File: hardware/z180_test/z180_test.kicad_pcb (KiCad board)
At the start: 2 copper layers, 48 parts, among them J1 Conn_01x04, J2 DIN41612_02x32_AB, J3 Conn_01x04, J4 Conn_01x06, J5 Conn_01x06, J6 Conn_02x17_Counter_Clockwise, SW1 SW_Push, U1 74AHC32, U10 8255A, U11 28C256, U12 AS6C4008-55PCN, U2 74LS244, U3 74LS244, U4 74LS244, U5 74LS245, U6 Z180, U7 74HC04, U8 74LS139, U9 74HC14, X1 OSC 12.288MHz 5V

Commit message: tentative placement
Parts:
- added C12: .01uF, Capacitor_THT:C_Disc_D5.0mm_W2.5mm_P2.50mm, F.Cu at (144.8, 45.7)
- added C13: .01uF, Capacitor_THT:C_Disc_D5.0mm_W2.5mm_P2.50mm, F.Cu at (132.0, 43.2)
- added C14: .01uF, Capacitor_THT:C_Disc_D5.0mm_W2.5mm_P2.50mm, F.Cu at (119.4, 45.7)
- X1: value OSC 12.288MHz 5V -> ACO-xxxMHz-A; footprint Oscillator:Oscillator_SeikoEpson_SG-8002DC -> Oscillator:Oscillator_DIP-14
- moved SW1 129.8 mm to (181.6, 38.1)
- moved J1 115.2 mm to (59.7, 36.8), turned to 90 degrees
- moved C11 108.9 mm to (177.8, 58.4), turned to 180 degrees
- moved C5 107.0 mm to (157.5, 45.7), turned to 180 degrees
- moved D3 101.3 mm to (129.5, 33.0)
- moved J4 100.0 mm to (88.9, 137.2), turned to 90 degrees
- moved R10 92.7 mm to (146.1, 38.1), turned to 180 degrees
- moved J5 89.8 mm to (114.3, 137.2), turned to 90 degrees
- moved U5 87.8 mm to (63.5, 106.7), turned to 180 degrees
- moved U10 86.0 mm to (168.9, 63.5)
- moved C8 82.9 mm to (129.5, 38.1)
- moved C10 80.1 mm to (156.2, 73.7), turned to 180 degrees
- moved U8 79.8 mm to (127.0, 48.3)
- moved R12 79.4 mm to (146.1, 121.9), turned to 180 degrees
- moved R1 69.9 mm to (55.9, 123.2)
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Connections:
- X1 pad 8: VCC -> Net-(U6-EXTAL)
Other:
- board outline added: 177.8 x 114.3 mm

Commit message: placement
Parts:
- added H1: MountingHole, MountingHolesInch:Mtg4-40, F.Cu at (27.9, 31.8)
- added H2: MountingHole, MountingHolesInch:Mtg4-40, F.Cu at (27.9, 138.4)
- added H3: MountingHole, MountingHolesInch:Mtg4-40, F.Cu at (240.0, 31.8)
- added H4: MountingHole, MountingHolesInch:Mtg4-40, F.Cu at (240.0, 138.4)
- added H5: MountingHole, MountingHolesInch:Mtg4-40, F.Cu at (86.4, 138.4)
- added H6: MountingHole, MountingHolesInch:Mtg4-40, F.Cu at (86.4, 31.8)
- added H7: MountingHole, MountingHolesInch:Mtg4-40, F.Cu at (153.7, 31.8)
- added H8: MountingHole, MountingHolesInch:Mtg4-40, F.Cu at (195.6, 138.4)
- added J7: DIN41612_02x32_AB, Connector_DIN:DIN41612_B_2x32_Female_Vertical_THT, F.Cu at (35.6, 47.0)
- added J8: DIN41612_02x32_AB, Connector_DIN:DIN41612_B_2x32_Female_Vertical_THT, F.Cu at (54.6, 47.0)
- J1: footprint Connector_PinHeader_2.54mm:PinHeader_1x04_P2.54mm_Vertical -> Connector_Molex:Molex_KK-396_A-41791-0004_1x04_P3.96mm_Vertical
- moved SW1 93.2 mm to (219.7, 123.2)
- moved J1 57.3 mm to (117.0, 34.3), turned to 180 degrees
- moved C5 38.1 mm to (195.6, 45.7)
- moved C7 38.1 mm to (174.0, 69.8)
- moved U9 38.1 mm to (177.8, 50.8)
- moved C9 38.1 mm to (109.3, 78.7)
- moved J5 38.1 mm to (152.4, 137.2)
- moved R11 38.1 mm to (146.1, 121.9)
- moved R3 38.1 mm to (132.1, 71.1)
- moved R4 38.1 mm to (121.9, 118.1)
- moved R5 38.1 mm to (121.9, 121.9)
- moved R6 38.1 mm to (132.1, 125.7)
- moved U6 38.1 mm to (156.2, 92.7)
- moved X1 38.1 mm to (132.1, 49.5)
- moved D1 38.1 mm to (99.1, 134.6)
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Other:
- board size 177.8 x 114.3 mm -> 219.7 x 114.3 mm
- copper layers 2 -> 4

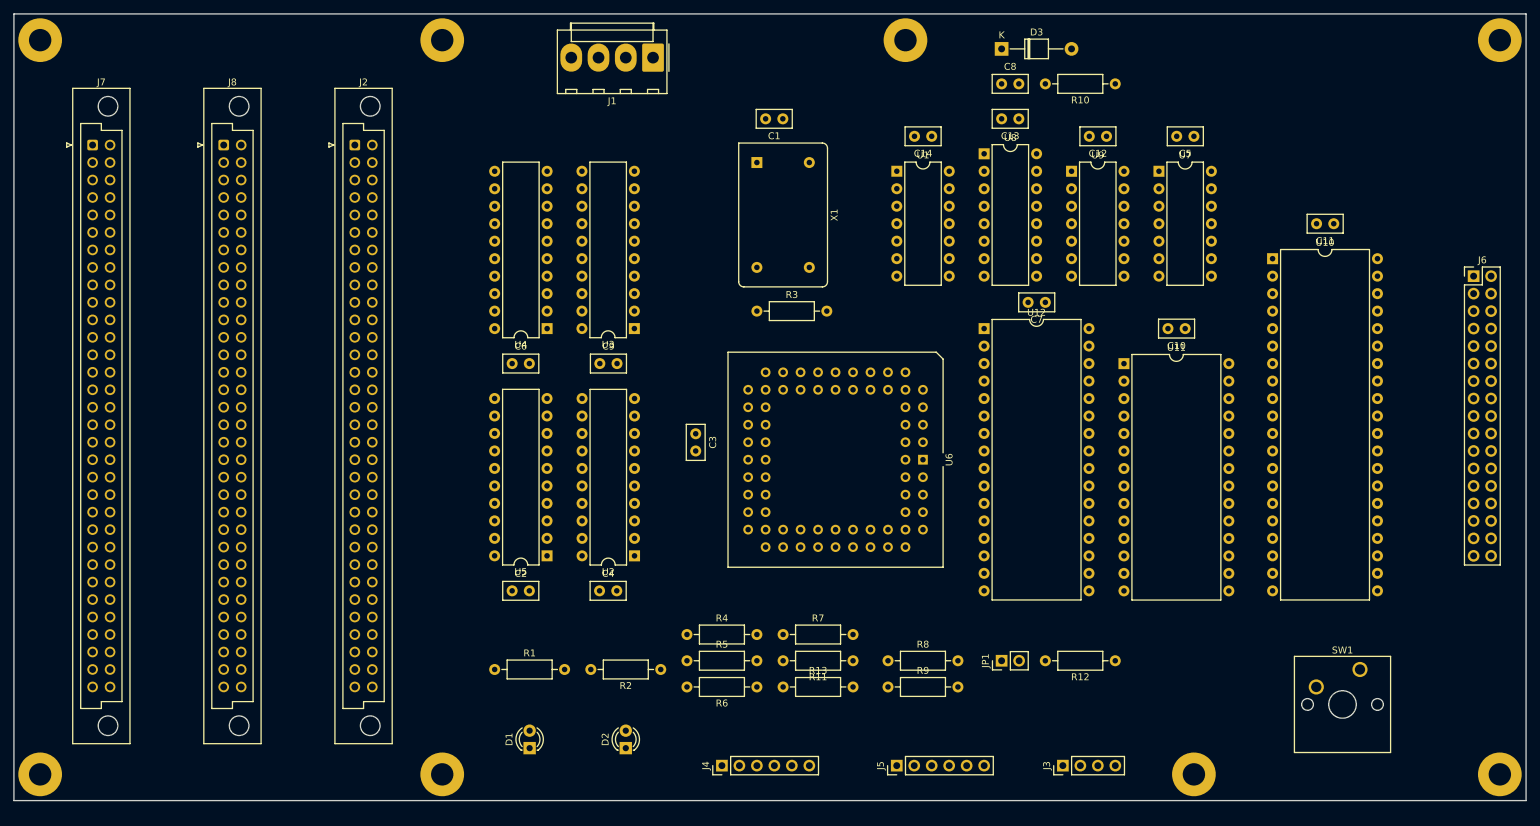
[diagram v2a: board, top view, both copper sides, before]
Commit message: add VR
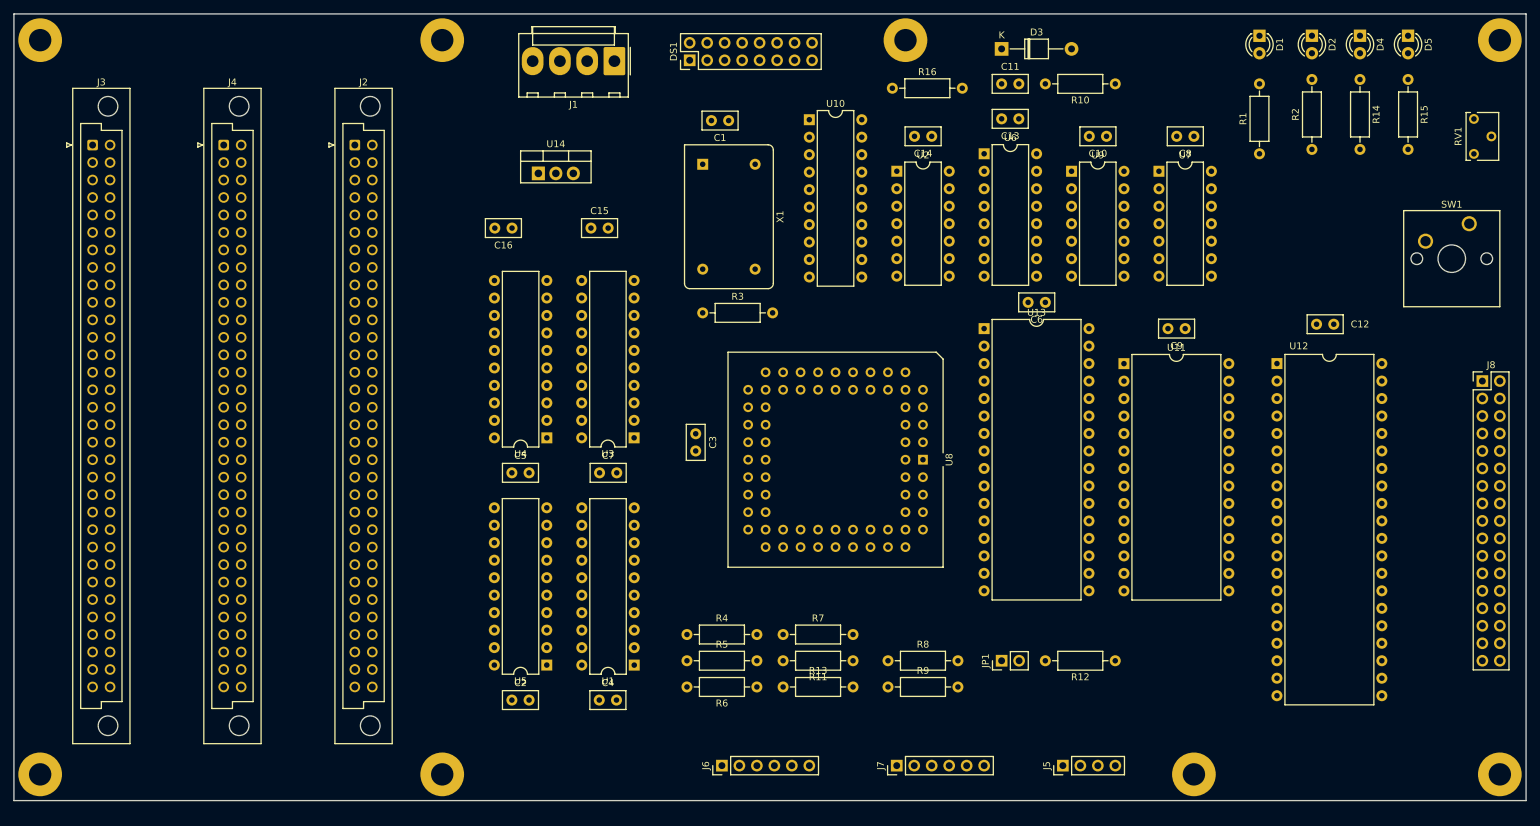
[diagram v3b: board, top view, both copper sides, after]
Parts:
- added C15: .01uF, Capacitor_THT:C_Disc_D5.0mm_W2.5mm_P2.50mm, F.Cu at (108.0, 59.1)
- added C16: .01uF, Capacitor_THT:C_Disc_D5.0mm_W2.5mm_P2.50mm, F.Cu at (96.5, 59.1)
- added D4: LED, LED_THT:LED_D3.0mm, F.Cu at (219.7, 31.1)
- added D5: LED, LED_THT:LED_D3.0mm, F.Cu at (226.7, 31.1)
- added DS1: RC1602A, Connector_PinHeader_2.54mm:PinHeader_2x08_P2.54mm_Vertical, F.Cu at (122.3, 34.7)
- added R14: 1k, Resistor_THT:R_Axial_DIN0207_L6.3mm_D2.5mm_P10.16mm_Horizontal, F.Cu at (219.7, 37.5)
- added R15: 1k, Resistor_THT:R_Axial_DIN0207_L6.3mm_D2.5mm_P10.16mm_Horizontal, F.Cu at (226.7, 37.5)
- added R16: 470, Resistor_THT:R_Axial_DIN0207_L6.3mm_D2.5mm_P10.16mm_Horizontal, F.Cu at (151.8, 38.7)
- added RV1: 10k, Potentiometer_THT:Potentiometer_Bourns_3266W_Vertical, F.Cu at (236.3, 43.2)
- added U10: 74LS374, Package_DIP:DIP-20_W7.62mm, F.Cu at (139.7, 43.3)
- added U14: LM7805_TO220, Package_TO_SOT_THT:TO-220-3_Vertical, F.Cu at (100.3, 51.1)
- moved D1 148.2 mm to (205.1, 31.1), turned to -90 degrees
- moved D2 143.7 mm to (212.7, 31.1), turned to -90 degrees
- moved R1 134.0 mm to (205.1, 48.3), turned to 90 degrees
- moved R2 121.1 mm to (212.7, 47.6), turned to 90 degrees
- moved SW1 66.7 mm to (235.6, 58.4)
- moved C2 15.9 mm to (96.5, 127.6)
- moved C4 15.9 mm to (109.2, 127.6)
- moved C5 15.9 mm to (96.5, 94.6)
- moved C7 15.9 mm to (109.2, 94.6)
- moved U1 15.9 mm to (114.3, 122.6)
- moved U3 15.9 mm to (114.2, 89.5)
- moved U4 15.9 mm to (101.6, 89.5)
- moved U5 15.9 mm to (101.5, 122.5)
- moved J8 15.3 mm to (237.5, 81.3)
- moved U12 15.3 mm to (207.6, 78.7)
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- renumbered C12 to C10, C8 to C11, C11 to C12, C6 to C5, C7 to C6, C9 to C7, C5 to C8, C10 to C9, J7 to J3, J8 to J4, J3 to J5, J4 to J6, J5 to J7, J6 to J8, U2 to U1, U10 to U12, U12 to U13, U1 to U2, U8 to U6, U6 to U8
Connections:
- J1 pad 1: VCC -> Net-(J1-Pin_1)
- J1 pad 2: VCC -> Net-(J1-Pin_1)
- U6 pad 9: unconnected-(U8B-O3-Pad9) -> /nLCD

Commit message: tweaking placement
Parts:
- moved D5 3.70 mm to (228.6, 34.3)
- moved R15 3.70 mm to (228.6, 40.6)
- moved D4 3.42 mm to (221.0, 34.3)
- moved R14 3.42 mm to (221.0, 40.6)
- moved R1 3.24 mm to (204.5, 51.4)
- moved D1 3.24 mm to (204.5, 34.3)
- moved D2 3.17 mm to (212.7, 34.3)
- moved R2 3.17 mm to (212.7, 50.8)
- moved RV1 2.54 mm to (238.8, 43.2)
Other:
- board text added: "HALT"
- board text added: "LED1"
- board text added: "LED2"
- board text added: "LED3"
- board text added: "Port A"
- board text added: "Port B"
- board text added: "RESET"
- board text added: "Sync"
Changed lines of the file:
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@@
 	(footprint "LED_THT:LED_D3.0mm"
 		(layer "F.Cu")
-		(at 226.695 31.11 -90)
+		(at 228.6 34.285 -90)
 		(descr "LED, diameter 3.0mm, 2 pins")
 		(tags "LED diameter 3.0mm 2 pins")
@@
 		(tags "C Disc series Radial pin pitch 2.50mm  diameter 5mm width 2.5mm Capacitor")
 		(property "Reference" "C15"
-			(at 1.25 -2.5 360)
+			(at 1.25 -2.5 0)
 			(layer "F.SilkS")
 			(effects
@@
 		)
 		(property "Value" ".01uF"
-			(at 1.25 2.5 360)
+			(at 1.25 2.5 0)
 			(layer "F.Fab")
 			(effects
@@
 		)
 		(fp_text user "${REFERENCE}"
-			(at 1.25 0 360)
+			(at 1.25 0 0)
 			(layer "F.Fab")
 			(effects
@@
 	(footprint "LED_THT:LED_D3.0mm"
 		(layer "F.Cu")
-		(at 205.105 31.115 -90)
+		(at 204.47 34.29 -90)
 		(descr "LED, diameter 3.0mm, 2 pins")
 		(tags "LED diameter 3.0mm 2 pins")
@@
 	(footprint "LED_THT:LED_D3.0mm"
 		(layer "F.Cu")
-		(at 212.725 31.11 -90)
+		(at 212.725 34.285 -90)
 		(descr "LED, diameter 3.0mm, 2 pins")
 		(tags "LED diameter 3.0mm 2 pins")
@@
 	(footprint "Resistor_THT:R_Axial_DIN0207_L6.3mm_D2.5mm_P10.16mm_Horizontal"
 		(layer "F.Cu")
-		(at 205.105 48.26 90)
+		(at 204.47 51.435 90)
 		(descr "Resistor, Axial_DIN0207 series, Axial, Horizontal, pin pitch=10.16mm, 0.25W = 1/4W, length*diameter=6.3*2.5mm^2, http://cdn-reichelt.de/documents/datenblatt/B400/1_4W%23YAG.pdf")
 		(tags "Resistor Axial_DIN0207 series Axial Horizontal pin pitch 10.16mm 0.25W = 1/4W length 6.3mm diameter 2.5mm")
@@
 	(footprint "Resistor_THT:R_Axial_DIN0207_L6.3mm_D2.5mm_P10.16mm_Horizontal"
 		(layer "F.Cu")
-		(at 212.725 47.625 90)
+		(at 212.725 50.8 90)
 		(descr "Resistor, Axial_DIN0207 series, Axial, Horizontal, pin pitch=10.16mm, 0.25W = 1/4W, length*diameter=6.3*2.5mm^2, http://cdn-reichelt.de/documents/datenblatt/B400/1_4W%23YAG.pdf")
 		(tags "Resistor Axial_DIN0207 series Axial Horizontal pin pitch 10.16mm 0.25W = 1/4W length 6.3mm diameter 2.5mm")
@@
 		(tags "C Disc series Radial pin pitch 2.50mm  diameter 5mm width 2.5mm Capacitor")
 		(property "Reference" "C16"
-			(at 1.25 -2.5 360)
+			(at 1.25 -2.5 0)
 			(layer "F.SilkS")
 			(effects
@@
 		)
 		(property "Value" ".01uF"
-			(at 1.25 2.5 360)
+			(at 1.25 2.5 0)
 			(layer "F.Fab")
 			(effects
@@
 		)
 		(fp_text user "${REFERENCE}"
-			(at 1.25 0 360)
+			(at 1.25 0 0)
 			(layer "F.Fab")
 			(effects
@@
 	(footprint "Potentiometer_THT:Potentiometer_Bourns_3266W_Vertical"
 		(layer "F.Cu")
-		(at 236.265 43.195 90)
+		(at 238.805 43.195 90)
 		(descr "Potentiometer, vertical, Bourns 3266W, https://www.bourns.com/docs/Product-Datasheets/3266.pdf")
 		(tags "Potentiometer vertical Bourns 3266W")
@@
 	(footprint "Resistor_THT:R_Axial_DIN0207_L6.3mm_D2.5mm_P10.16mm_Horizontal"
 		(layer "F.Cu")
-		(at 226.695 37.465 -90)
+		(at 228.6 40.64 -90)
 		(descr "Resistor, Axial_DIN0207 series, Axial, Horizontal, pin pitch=10.16mm, 0.25W = 1/4W, length*diameter=6.3*2.5mm^2, http://cdn-reichelt.de/documents/datenblatt/B400/1_4W%23YAG.pdf")
 		(tags "Resistor Axial_DIN0207 series Axial Horizontal pin pitch 10.16mm 0.25W = 1/4W length 6.3mm diameter 2.5mm")
@@
 	(footprint "LED_THT:LED_D3.0mm"
 		(layer "F.Cu")
-		(at 219.71 31.11 -90)
+		(at 220.98 34.285 -90)
 		(descr "LED, diameter 3.0mm, 2 pins")
 		(tags "LED diameter 3.0mm 2 pins")
@@
 		(tags "Resistor Axial_DIN0207 series Axial Horizontal pin pitch 10.16mm 0.25W = 1/4W length 6.3mm diameter 2.5mm")
 		(property "Reference" "R16"
-			(at 5.08 -2.37 360)
+			(at 5.08 -2.37 0)
 			(layer "F.SilkS")
 			(effects
@@
 		)
 		(property "Value" "470"
-			(at 5.08 2.37 360)
+			(at 5.08 2.37 0)
 			(layer "F.Fab")
 			(effects
@@
 		)
 		(fp_text user "${REFERENCE}"
-			(at 5.08 0 360)
+			(at 5.08 0 0)
 			(layer "F.Fab")
 			(effects
@@
 	(footprint "Resistor_THT:R_Axial_DIN0207_L6.3mm_D2.5mm_P10.16mm_Horizontal"
 		(layer "F.Cu")
-		(at 219.71 37.465 -90)
+		(at 220.98 40.64 -90)
 		(descr "Resistor, Axial_DIN0207 series, Axial, Horizontal, pin pitch=10.16mm, 0.25W = 1/4W, length*diameter=6.3*2.5mm^2, http://cdn-reichelt.de/documents/datenblatt/B400/1_4W%23YAG.pdf")
 		(tags "Resistor Axial_DIN0207 series Axial Horizontal pin pitch 10.16mm 0.25W = 1/4W length 6.3mm diameter 2.5mm")
@@
 		(layer "Edge.Cuts")
 	)
+	(gr_text "RESET"
+		(at 213.995 64.135 0)
+		(layer "F.SilkS")
+		(effects
+			(font
+				(size 1.905 1.905)
+				(thickness 0.2032)
+			)
+			(justify left bottom)
+		)
+	)
+	(gr_text "LED1"
+		(at 209.55 32.385 0)
+		(layer "F.SilkS")
+		(effects
+			(font
+				(size 1.905 1.905)
+				(thickness 0.2032)
+			)
+			(justify left bottom)
+		)
+	)
+	(gr_text "HALT"
+		(at 201.295 32.385 0)
+		(layer "F.SilkS")
+		(effects
+			(font
+				(size 1.905 1.905)
+				(thickness 0.2032)
+			)
+			(justify left bottom)
+		)
+	)
+	(gr_text "LED3"
+		(at 225.425 32.385 0)
+		(layer "F.SilkS")
+		(effects
+			(font
+				(size 1.905 1.905)
+				(thickness 0.2032)
+			)
+			(justify left bottom)
+		)
+	)
+	(gr_text "Port A"
+		(at 129.54 134.62 0)
+		(layer "F.SilkS")
+		(effects
+			(font
+				(size 1.905 1.905)
+				(thickness 0.2032)
+			)
+			(justify left bottom)
+		)
+	)
+	(gr_text "Port B"
+		(at 154.305 133.985 0)
+		(layer "F.SilkS")
+		(effects
+			(font
+				(size 1.905 1.905)
+				(thickness 0.2032)
+			)
+			(justify left bottom)
+		)
+	)
+	(gr_text "LED2"
+		(at 217.805 32.385 0)
+		(layer "F.SilkS")
+		(effects
+			(font
+				(size 1.905 1.905)
+				(thickness 0.2032)
+			)
+			(justify left bottom)
+		)
+	)
+	(gr_text "Sync"
+		(at 175.895 133.985 0)
+		(layer "F.SilkS")
+		(effects
+			(font
+				(size 1.905 1.905)
+				(thickness 0.2032)
+			)
+			(justify left bottom)
+		)
+	)
 )
